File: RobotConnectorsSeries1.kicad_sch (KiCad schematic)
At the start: 8 parts

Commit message: Prepare v0.2
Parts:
- S1-J17: footprint local_Connectors:Molex_Mini-Fit_Jr_5566-16A_2x08_P4.20mm_Vertical -> local_Connectors:CONN-TH_X9357WV-2X08HN-N2SN; Alternative (none) -> XKB Connection X9357WV-2x08HN-N2SN. ATTENTION: Different Fo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; JLC C5339222 -> C388779
- S1-J2: footprint local_Connectors:PinHeader_2x20_P1.27mm_R2.54mm_Vertical -> local_Connectors:AMPMODU System 50_2x20_P1.27mm_R2.54mm_Vertical
- S1-J3: footprint local_Connectors:PinHeader_2x10_P1.27mm_R2.54mm_Vertical -> local_Connectors:AMPMODU System50_2x10_P1.27mm_R2.54mm_Vertical
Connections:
- net GND: now also S1-J3.11 (Pin_11), S1-J3.13 (Pin_13), S1-J3.15 (Pin_15), S1-J3.17 (Pin_17), S1-J3.19 (Pin_19), S1-J3.9 (Pin_9); no longer S1-J2.15 (Pin_15)
- net LCD_IN_Z_5V: now reaches S1-J3.12 (Pin_12)
- net LCD_IN_Y_5V: now reaches S1-J3.16 (Pin_16)
- net LCD_IN_X_5V: now reaches S1-J3.20 (Pin_20)
- net BTN_SELECT: now reaches S1-J2.11 (Pin_11)
- net BTN_UP: now reaches S1-J2.12 (Pin_12)
- net BTN_PLAY: now reaches S1-J2.13 (Pin_13)
- net BTN_LEFT: now reaches S1-J2.14 (Pin_14)
- net BTN_MENU: now reaches S1-J2.17 (Pin_17)
- net SPK_PLUS: now reaches S1-J2.26 (Pin_26)
- net SPK_MINUS: now reaches S1-J2.27 (Pin_27)
- net LED_AUTO: now reaches S1-J2.30 (Pin_30)
- net LED_MOW: now reaches S1-J2.31 (Pin_31)
- net LED_HOME: now reaches S1-J2.32 (Pin_32)
- net LED_PWR: now reaches S1-J2.34 (Pin_34)
- net LED_PWR: now also S1-J2.40 (Pin_40)
- net LED_PLAY_GN: now reaches S1-J2.35 (Pin_35)
- net LED_PLAY_RD: now reaches S1-J2.36 (Pin_36)
- net BTN_BACK: now reaches S1-J2.5 (Pin_5)
- net BTN_DOWN: now reaches S1-J2.6 (Pin_6)
- net BTN_RIGHT: now reaches S1-J2.7 (Pin_7)
- net BTN_OK: now reaches S1-J2.8 (Pin_8)
- new net UI_~{CON}: S1-J2.15 (Pin_15)
- no-connect marks 81 -> 54
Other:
- moved on the sheet: S1-J2

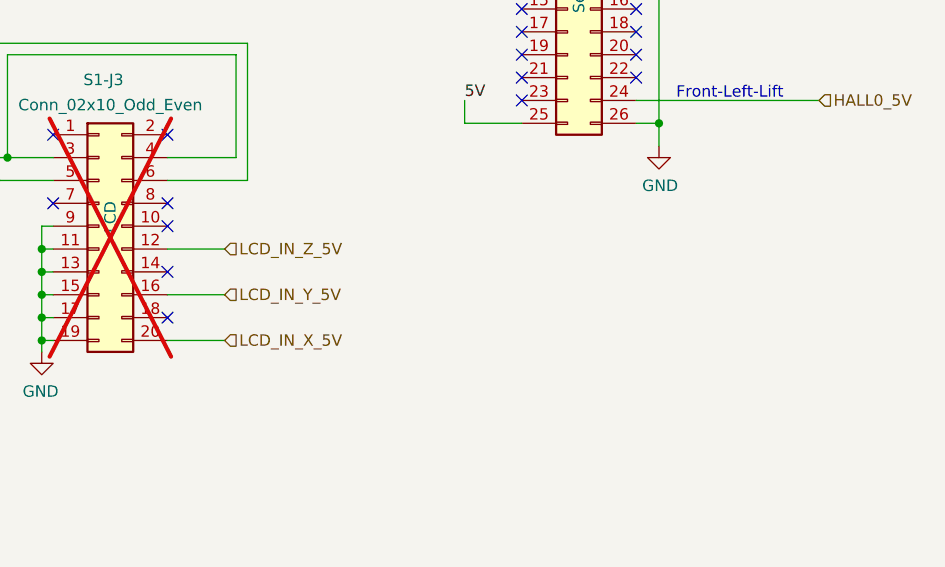
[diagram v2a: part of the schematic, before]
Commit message: Finish v0.2 schematic and ERC
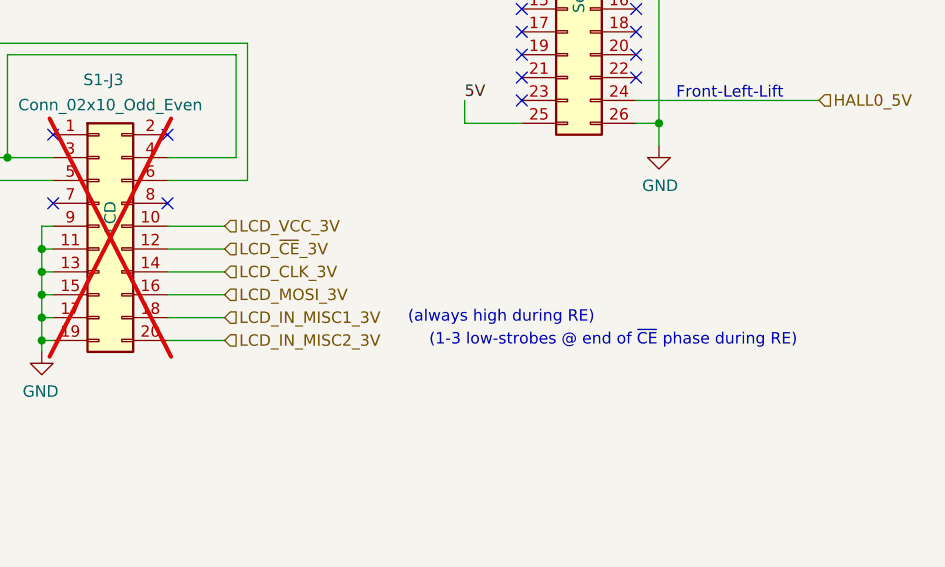
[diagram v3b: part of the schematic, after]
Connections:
- net LCD_VCC_3V: now reaches S1-J3.10 (Pin_10)
- net LCD_CLK_3V: now reaches S1-J3.14 (Pin_14)
- net LCD_IN_MISC1_3V: now reaches S1-J3.18 (Pin_18)
- net LCD_IN_X_5V renamed LCD_IN_MISC2_3V
- net LCD_IN_Y_5V renamed LCD_MOSI_3V
- net LCD_IN_Z_5V renamed LCD_~{CE}_3V
- no-connect marks 54 -> 51
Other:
- note added: "(1-3 low-strobes @ end of ~{CE} phase during RE)"
- note added: "(always high during RE)"
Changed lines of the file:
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@@
 	(title_block
 		(title "OpenMower SABO Mainboard for Series I & II")
-		(date "2025-05-04")
+		(date "2025-05-22")
 		(rev "v0.2")
 		(company "Apeheanger <joerg@ebeling.ws> for OpenMower")
@@
 		)
 	)
+	(text "(1-3 low-strobes @ end of ~{CE} phase during RE)"
+		(exclude_from_sim no)
+		(at 248.92 118.11 0)
+		(effects
+			(font
+				(size 1.27 1.27)
+			)
+		)
+	)
 	(text "W"
 		(exclude_from_sim no)
@@
 		(exclude_from_sim no)
 		(at 59.944 34.798 0)
+		(effects
+			(font
+				(size 1.27 1.27)
+			)
+		)
+	)
+	(text "(always high during RE)"
+		(exclude_from_sim no)
+		(at 236.474 115.57 0)
 		(effects
 			(font
@@
 	)
 	(no_connect
-		(at 199.39 115.57)
-	)
-	(no_connect
 		(at 64.77 48.26)
 	)
@@
 	)
 	(no_connect
-		(at 199.39 110.49)
-	)
-	(no_connect
 		(at 77.47 43.18)
 	)
@@
 	(no_connect
 		(at 238.76 66.04)
-	)
-	(no_connect
-		(at 199.39 105.41)
 	)
 	(no_connect
@@
 	(wire
 		(pts
+			(xy 199.39 115.57) (xy 205.74 115.57)
+		)
+		(stroke
+			(width 0)
+			(type default)
+		)
+	)
+	(wire
+		(pts
 			(xy 77.47 48.26) (xy 81.28 48.26)
 		)
@@
 	(wire
 		(pts
+			(xy 199.39 105.41) (xy 205.74 105.41)
+		)
+		(stroke
+			(width 0)
+			(type default)
+		)
+	)
+	(wire
+		(pts
 			(xy 62.23 87.63) (xy 62.23 85.09)
 		)
@@
 		(pts
 			(xy 184.15 69.85) (xy 184.15 72.39)
+		)
+		(stroke
+			(width 0)
+			(type default)
+		)
+	)
+	(wire
+		(pts
+			(xy 199.39 110.49) (xy 205.74 110.49)
 		)
 		(stroke
@@
 		)
 	)
+	(hierarchical_label "LCD_CLK_3V"
+		(shape input)
+		(at 205.74 110.49 0)
+		(effects
+			(font
+				(size 1.27 1.27)
+			)
+			(justify left)
+		)
+	)
 	(hierarchical_label "BTN_LEFT"
 		(shape input)
@@
 		)
 	)
-	(hierarchical_label "LCD_IN_Z_5V"
+	(hierarchical_label "LCD_~{CE}_3V"
 		(shape input)
 		(at 205.74 107.95 0)
@@
 		)
 	)
-	(hierarchical_label "LCD_IN_X_5V"
+	(hierarchical_label "LCD_IN_MISC2_3V"
 		(shape input)
 		(at 205.74 118.11 0)
@@
 		)
 	)
-	(hierarchical_label "LCD_IN_Y_5V"
+	(hierarchical_label "LCD_MOSI_3V"
 		(shape input)
 		(at 205.74 113.03 0)
@@
 		(effects
 			(font
+				(size 1.27 1.27)
+			)
+			(justify left)
+		)
+	)
+	(hierarchical_label "LCD_VCC_3V"
+		(shape input)
+		(at 205.74 105.41 0)
+		(effects
+			(font
+				(size 1.27 1.27)
+			)
+			(justify left)
+		)
+	)
+	(hierarchical_label "LCD_IN_MISC1_3V"
+		(shape input)
+		(at 205.74 115.57 0)
+		(effects
+			(font

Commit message: Finish v0.2 PCB and DRC
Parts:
- S1-J17: footprint local_Connectors:CONN-TH_X9357WV-2X08HN-N2SN -> local_Connectors:Molex_Mini-Fit_Jr_5566-16A_2x08_P4.20mm_Vertical; Alternative XKB Connection X9357WV-2x08HN-N2SN. ATTENTION: Different Fo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 -> (none); JLC C388779 -> C5339222
- S1-J7: FT Rotation Offset 180 -> 0; LCSC Part # (none) -> C400369; MFPN MOLEX 430450818 -> 430450818; Manufacturer (none) -> Molex
- S1-J9: FT Rotation Offset (none) -> -90; LCSC Part # (none) -> C7501247; MFPN BHR-26-VUA -> ZX-IDC2.54-2-13PZZ; Manufacturer (none) -> Megastar
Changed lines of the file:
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@@
 			)
 		)
-		(property "Description" "Generic connector, double row, 02x13, odd/even pin numbering scheme (row 1 odd numbers, row 2 even numbers), script generated (kicad-library-utils/schlib/autogen/connector/)"
+		(property "Description" "2.54mm 260℃@10S -40℃~+105℃ Direct Insert 3A Gold Brass 1kV 2x13P 13 2.54mm Simple cow constellation 2 Plugin,P=2.54mm  IDC Connectors ROHS"
 			(at 243.84 78.74 0)
 			(effects
@@
 			)
 		)
-		(property "MFPN" "BHR-26-VUA"
+		(property "MFPN" "ZX-IDC2.54-2-13PZZ"
 			(at 243.84 78.74 0)
 			(effects
@@
 			)
 		)
-		(property "MPN" ""
+		(property "Manufacturer" "Megastar"
 			(at 243.84 78.74 0)
 			(effects
@@
 					(size 1.27 1.27)
 				)
+				(hide yes)
+			)
+		)
+		(property "LCSC Part #" "C7501247"
+			(at 243.84 78.74 0)
+			(effects
+				(font
+					(size 1.27 1.27)
+				)
+				(hide yes)
+			)
+		)
+		(property "FT Rotation Offset" "-90"
+			(at 243.84 78.74 0)
+			(effects
+				(font
+					(size 1.27 1.27)
+				)
+				(hide yes)
 			)
 		)
@@
 			)
 		)
-		(property "Description" "Generic connectable mounting pin connector, double row, 02x04, top/bottom pin numbering scheme (row 1: 1...pins_per_row, row2: pins_per_row+1 ... num_pins), script generated (kicad-library-utils/schlib/autogen/connector/)"
+		(property "Description" "2x4P 8P Micro-Fit(MX 3.0) Tin 3mm 4 -40℃~+105℃ 8.5A 2 3mm Brass Standing paste SMD,P=3mm Wire To Board Connector ROHS"
 			(at 243.84 31.75 0)
 			(effects
@@
 			)
 		)
-		(property "MFPN" "MOLEX 430450818"
+		(property "Manufacturer" "Molex"
 			(at 243.84 31.75 0)
 			(effects
@@
 			)
 		)
-		(property "FT Rotation Offset" "180"
+		(property "MFPN" "430450818"
 			(at 243.84 31.75 0)
 			(effects
@@
 			)
 		)
-		(property "MPN" ""
+		(property "FT Rotation Offset" "0"
+			(at 243.84 31.75 0)
+			(effects
+				(font
+					(size 1.27 1.27)
+				)
+				(hide yes)
+			)
+		)
+		(property "LCSC Part #" "C400369"
 			(at 243.84 31.75 0)
 			(effects
@@
 			)
 		)
-		(property "Footprint" "local_Connectors:CONN-TH_X9357WV-2X08HN-N2SN"
+		(property "Footprint" "local_Connectors:Molex_Mini-Fit_Jr_5566-16A_2x08_P4.20mm_Vertical"
 			(at 69.85 43.18 0)
 			(effects
@@
 			)
 		)
-		(property "Alternative" "XKB Connection X9357WV-2x08HN-N2SN. ATTENTION: Different Footprint"
+		(property "JLC" "C5339222"
 			(at 69.85 43.18 0)
 			(effects
@@
 			)
 		)
-		(property "JLC" "C388779"
-			(at 69.85 43.18 0)
-			(effects
-				(font
-					(size 1.27 1.27)
-				)
-				(hide yes)
-			)
-		)
-		(property "MPN" ""
-			(at 69.85 43.18 0)
-			(effects
-				(font
-					(size 1.27 1.27)
-				)
-			)
-		)

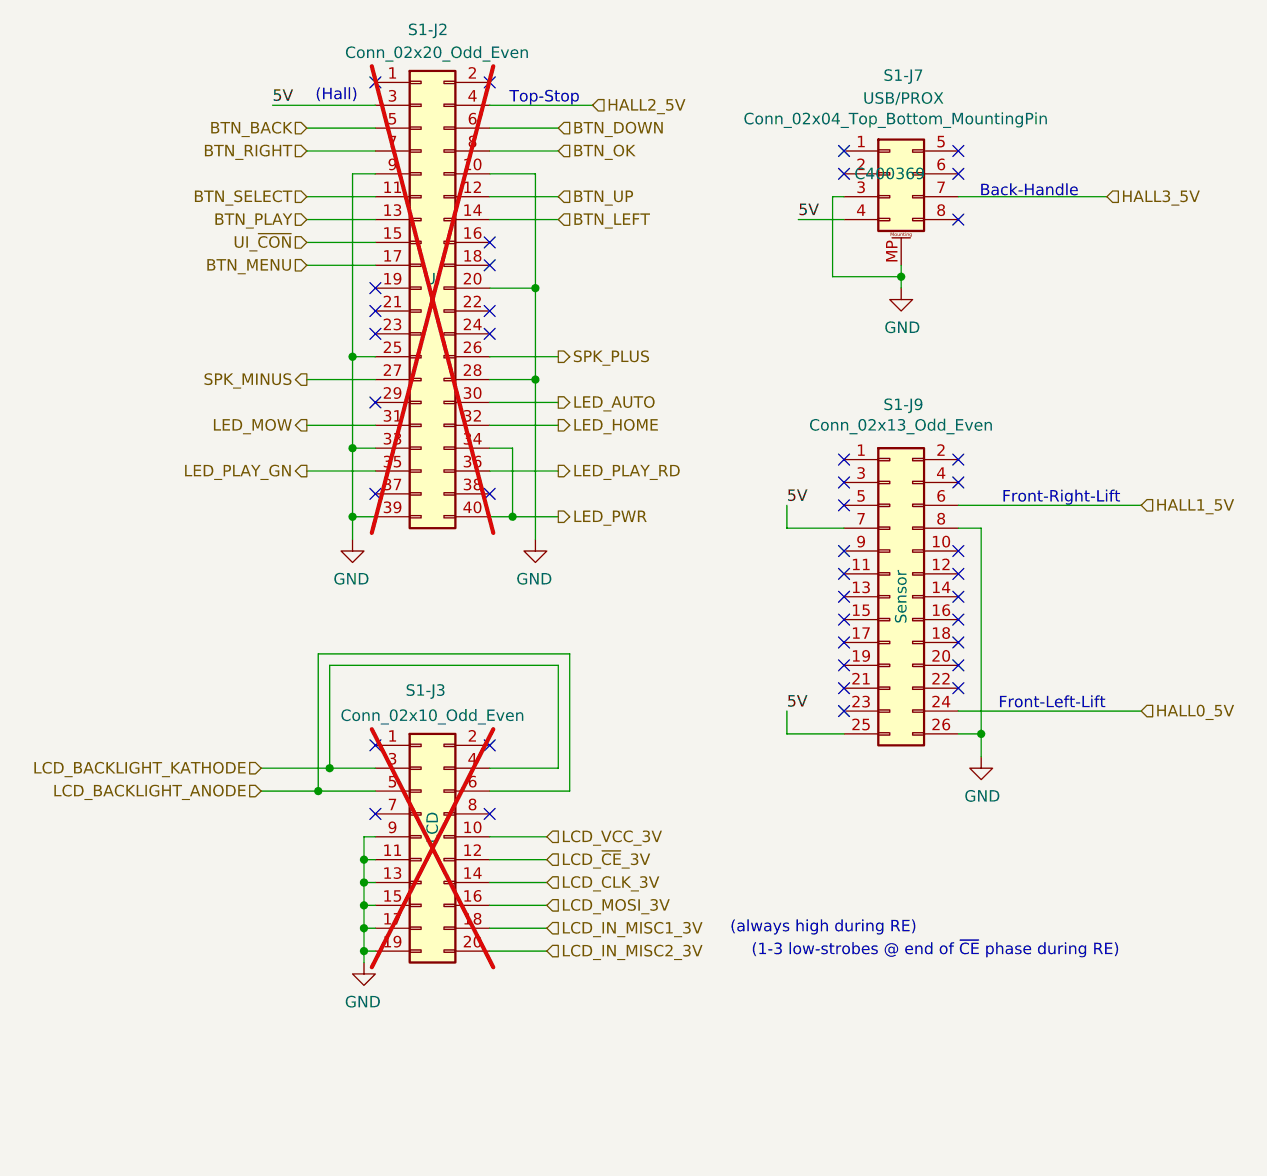
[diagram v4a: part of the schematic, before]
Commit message: Restructured v0.1 for easier worktree use
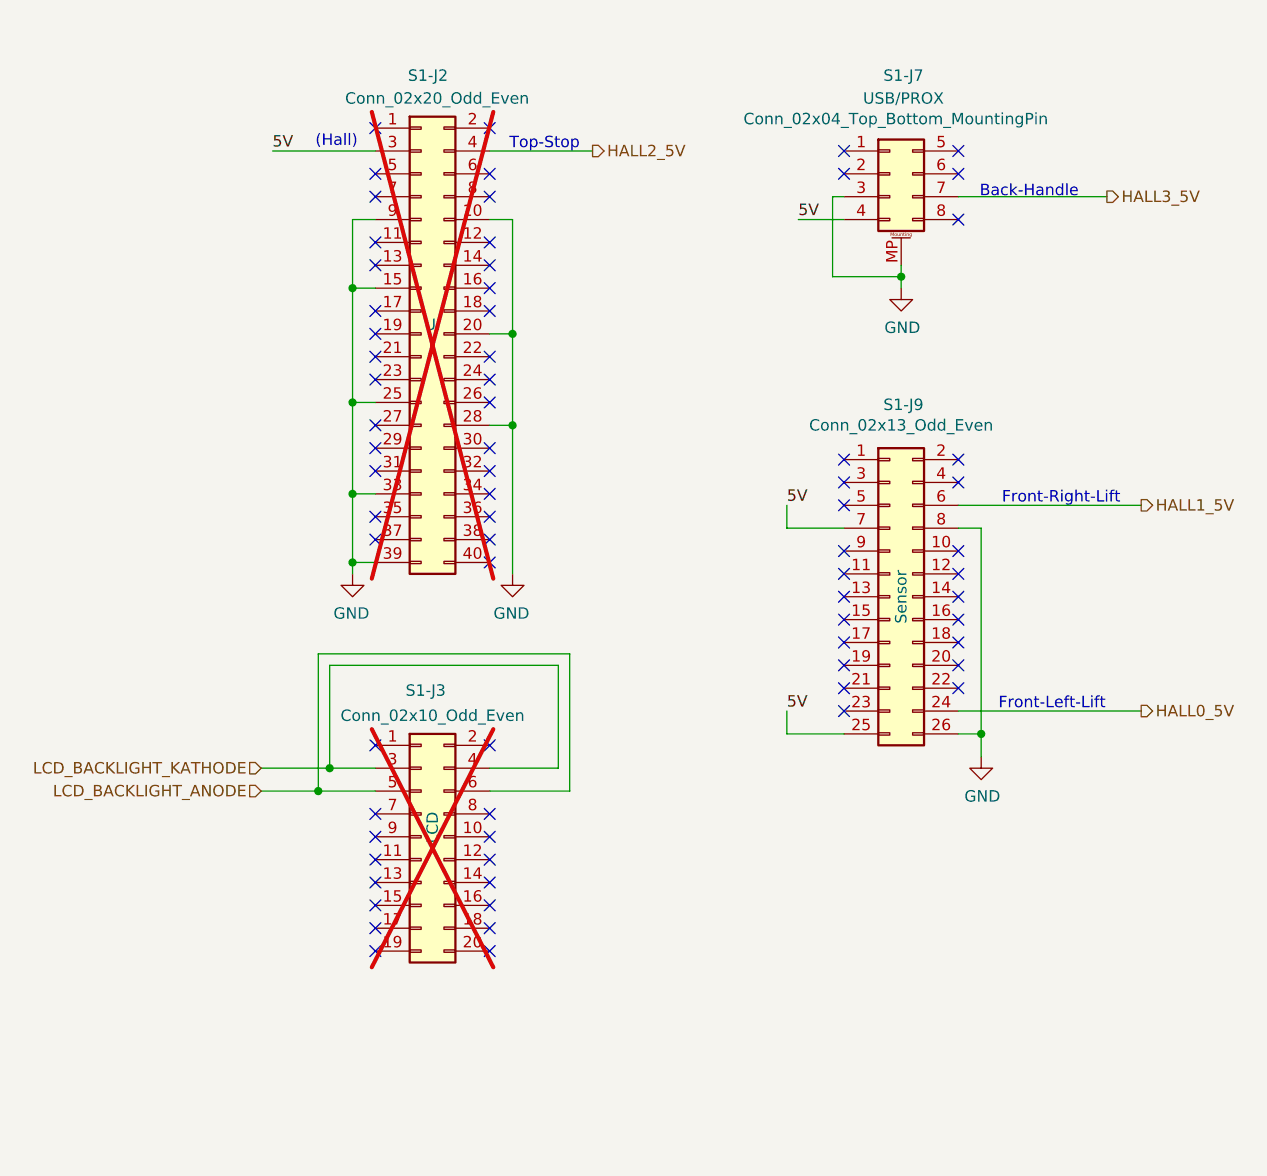
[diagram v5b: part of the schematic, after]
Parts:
- S1-J2: footprint local_Connectors:AMPMODU System 50_2x20_P1.27mm_R2.54mm_Vertical -> local_Connectors:PinHeader_2x20_P1.27mm_R2.54mm_Vertical
- S1-J3: footprint local_Connectors:AMPMODU System50_2x10_P1.27mm_R2.54mm_Vertical -> local_Connectors:PinHeader_2x10_P1.27mm_R2.54mm_Vertical
- S1-J7: FT Rotation Offset 0 -> 180; LCSC Part # C400369 -> (none); MFPN 430450818 -> MOLEX 430450818; Manufacturer Molex -> (none)
- S1-J9: FT Rotation Offset -90 -> (none); LCSC Part # C7501247 -> (none); MFPN ZX-IDC2.54-2-13PZZ -> BHR-26-VUA; Manufacturer Megastar -> (none)
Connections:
- net UI_~{CON} is gone; now on net GND: S1-J2.15 (Pin_15)
- net GND: no longer S1-J3.11 (Pin_11), S1-J3.13 (Pin_13), S1-J3.15 (Pin_15), S1-J3.17 (Pin_17), S1-J3.19 (Pin_19), S1-J3.9 (Pin_9)
- net BTN_BACK: no longer names the net of S1-J2.5 (Pin_5)
- net BTN_DOWN: no longer names the net of S1-J2.6 (Pin_6)
- net BTN_LEFT: no longer names the net of S1-J2.14 (Pin_14)
- net BTN_MENU: no longer names the net of S1-J2.17 (Pin_17)
- net BTN_OK: no longer names the net of S1-J2.8 (Pin_8)
- net BTN_PLAY: no longer names the net of S1-J2.13 (Pin_13)
- net BTN_RIGHT: no longer names the net of S1-J2.7 (Pin_7)
- net BTN_SELECT: no longer names the net of S1-J2.11 (Pin_11)
- net BTN_UP: no longer names the net of S1-J2.12 (Pin_12)
- net LCD_CLK_3V: no longer names the net of S1-J3.14 (Pin_14)
- net LCD_IN_MISC1_3V: no longer names the net of S1-J3.18 (Pin_18)
- net LCD_IN_MISC2_3V: no longer names the net of S1-J3.20 (Pin_20)
- net LCD_MOSI_3V: no longer names the net of S1-J3.16 (Pin_16)
- net LCD_VCC_3V: no longer names the net of S1-J3.10 (Pin_10)
- net LCD_~{CE}_3V: no longer names the net of S1-J3.12 (Pin_12)
- net LED_AUTO: no longer names the net of S1-J2.30 (Pin_30)
- net LED_HOME: no longer names the net of S1-J2.32 (Pin_32)
- net LED_MOW: no longer names the net of S1-J2.31 (Pin_31)
- net LED_PLAY_GN: no longer names the net of S1-J2.35 (Pin_35)
- net LED_PLAY_RD: no longer names the net of S1-J2.36 (Pin_36)
- net LED_PWR: no longer names the net of S1-J2.34 (Pin_34)
- net LED_PWR: no longer S1-J2.40 (Pin_40)
- net SPK_MINUS: no longer names the net of S1-J2.27 (Pin_27)
- net SPK_PLUS: no longer names the net of S1-J2.26 (Pin_26)
- no-connect marks 51 -> 81
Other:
- note removed: "(1-3 low-strobes @ end of ~{CE} phase during RE)"
- note removed: "(always high during RE)"
- moved on the sheet: S1-J2
